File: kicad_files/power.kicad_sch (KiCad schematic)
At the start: 0 parts

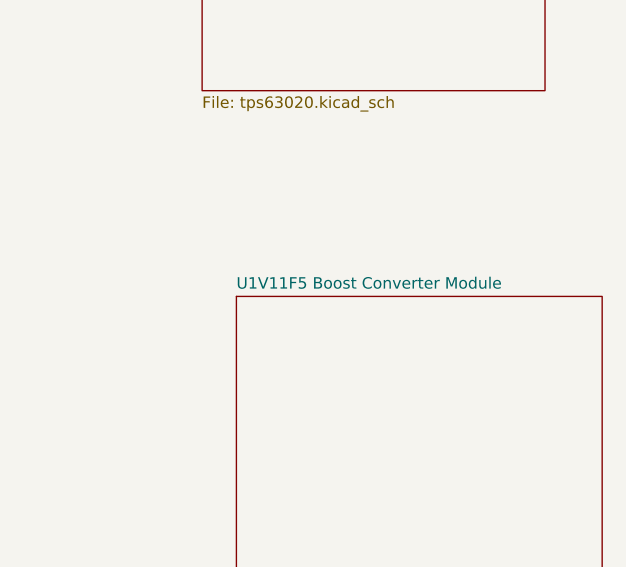
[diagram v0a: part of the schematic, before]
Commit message: Completed fuel gauge schematic based on application guidance provided in the LC709203F datasheet.
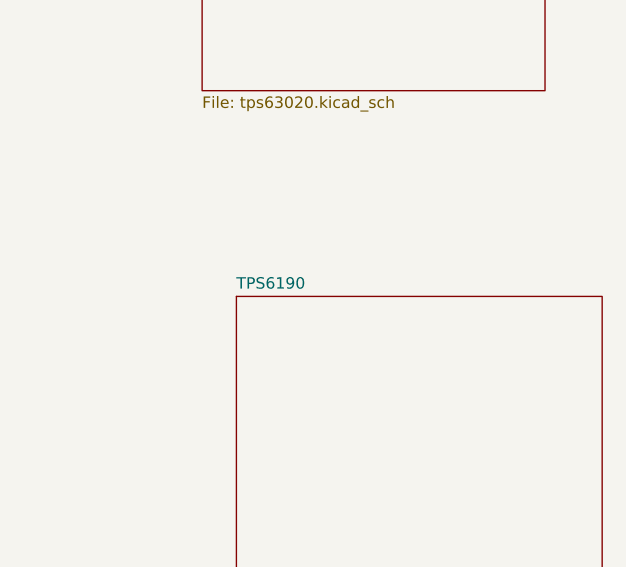
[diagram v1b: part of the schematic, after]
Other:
- sheet U1V11F5 Boost Converter Module renamed TPS6190
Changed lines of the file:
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@@
 			(color 0 0 0 0.0000)
 		)
-		(property "Sheetname" "U1V11F5 Boost Converter Module"
+		(property "Sheetname" "TPS6190"
 			(at 173.99 100.8884 0)
 			(effects

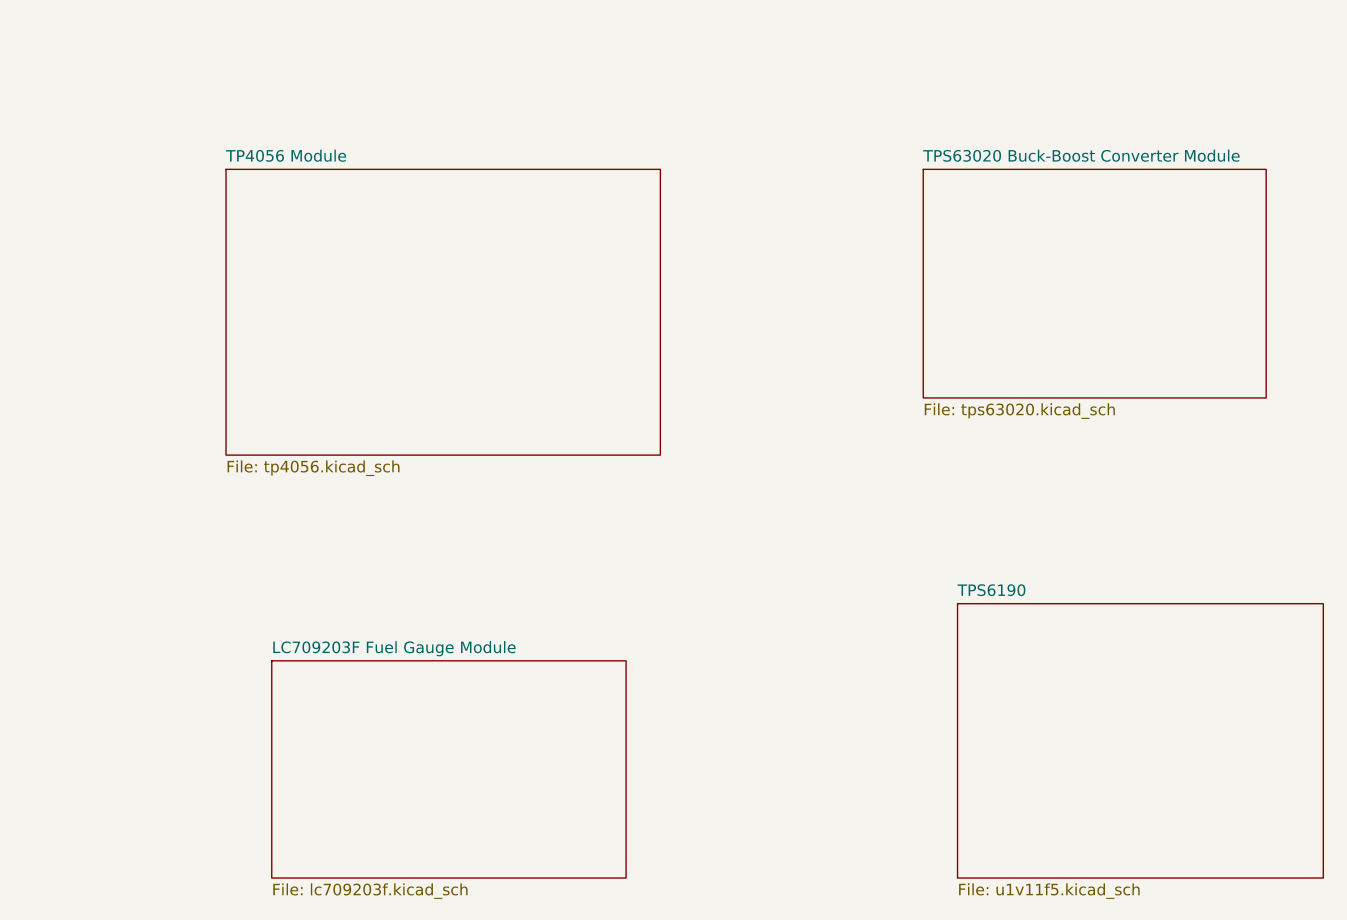
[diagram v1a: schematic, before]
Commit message: Revamped power subsystem design
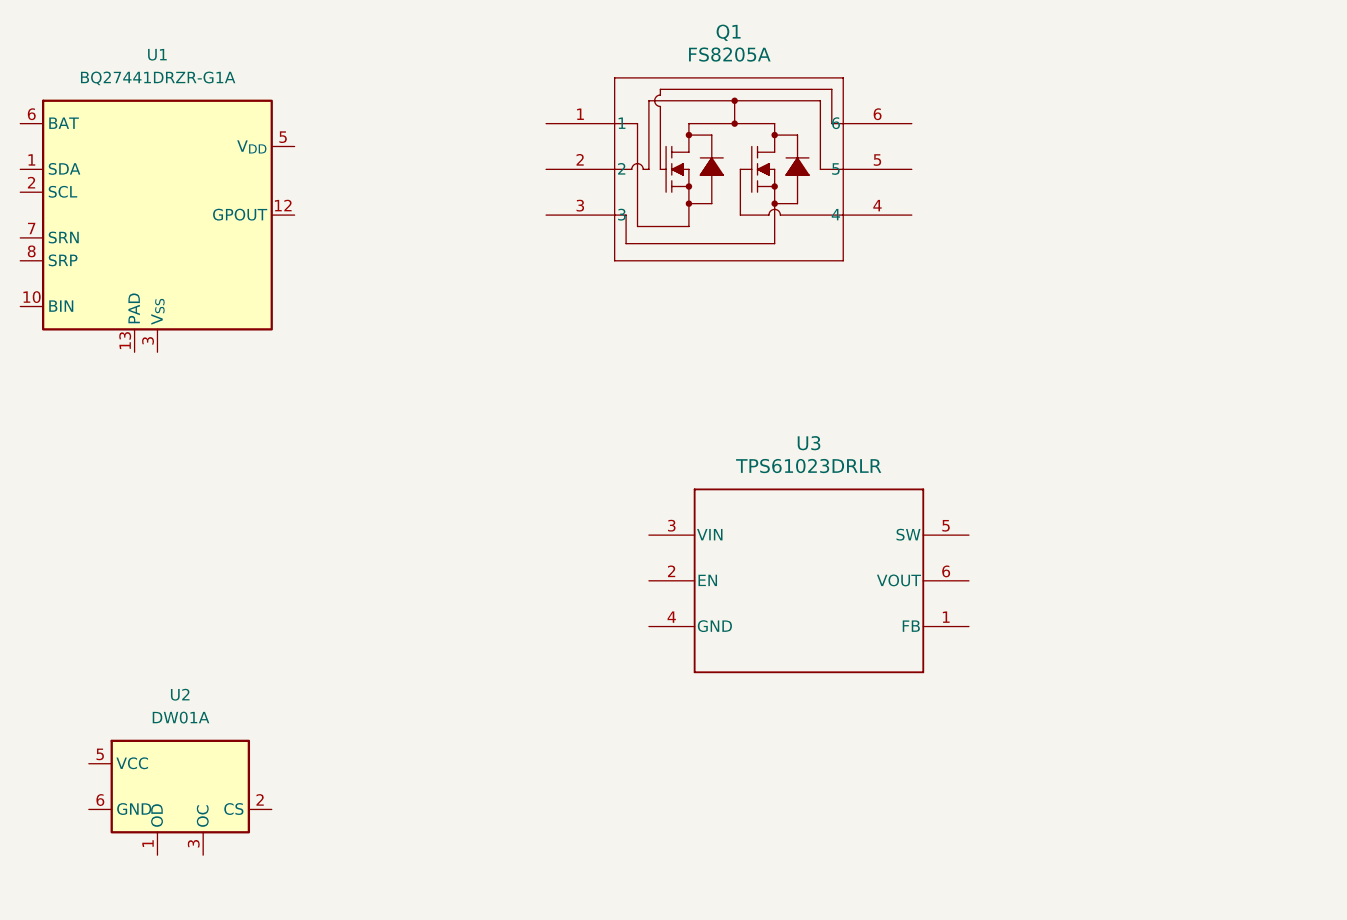
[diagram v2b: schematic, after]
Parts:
- added Q1: FS8205A, SOT-23-6L_TCP, symbol FS8205A:FS8205A
- added U1: BQ27441DRZR-G1A, Package_SON:Texas_S-PDSO-N12, symbol Battery_Management:BQ27441DRZR-G1A
- added U2: DW01A, Package_TO_SOT_SMD:SOT-23-6, symbol Battery_Management:DW01A
- added U3: TPS61023DRLR, DRL0006A, symbol TPS61023:TPS61023DRLR
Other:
- removed sheet LC709203F Fuel Gauge Module
- removed sheet TP4056 Module
- removed sheet TPS6190
- removed sheet TPS63020 Buck-Boost Converter Module

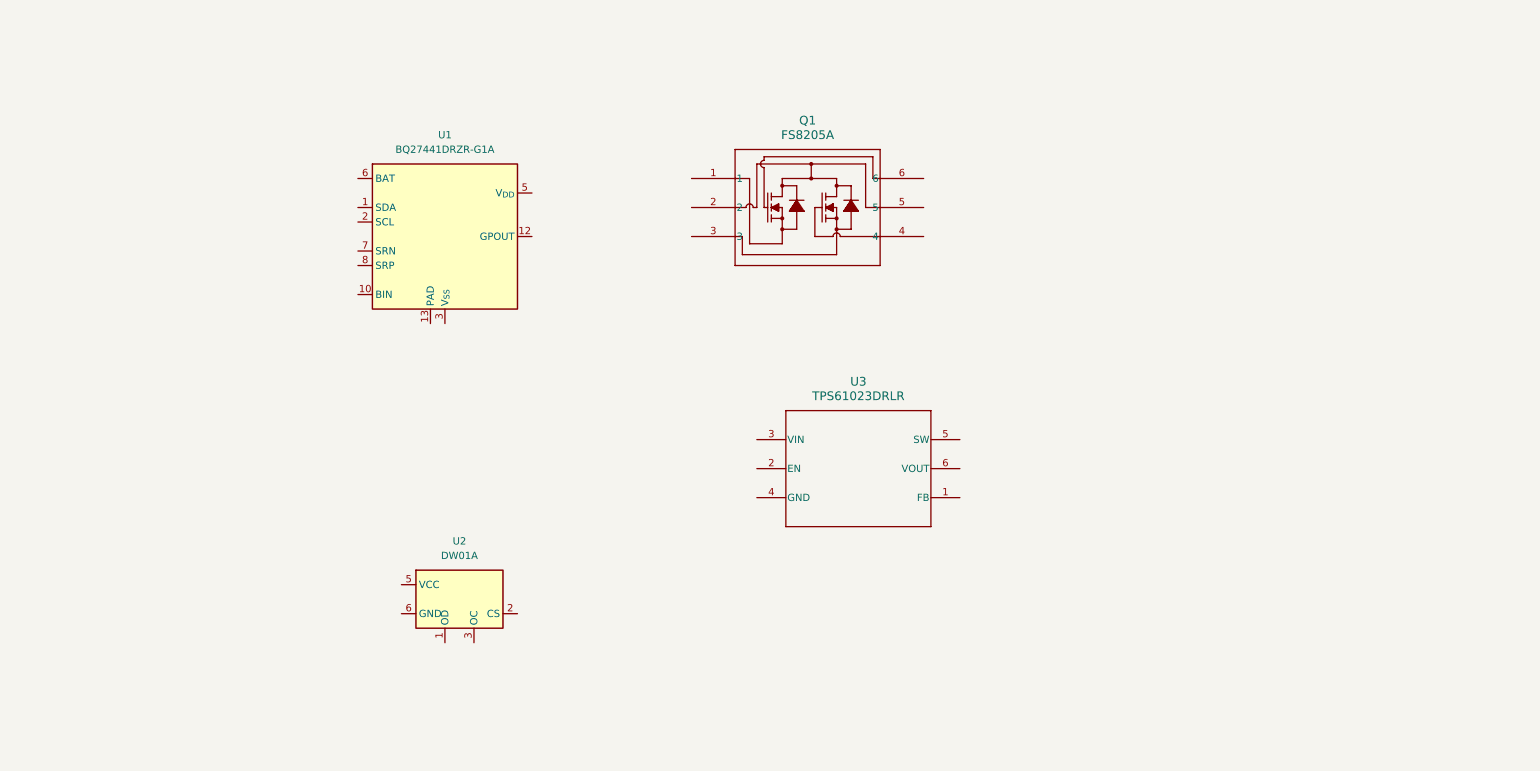
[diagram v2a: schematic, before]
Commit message: Protection portion of power subsystem
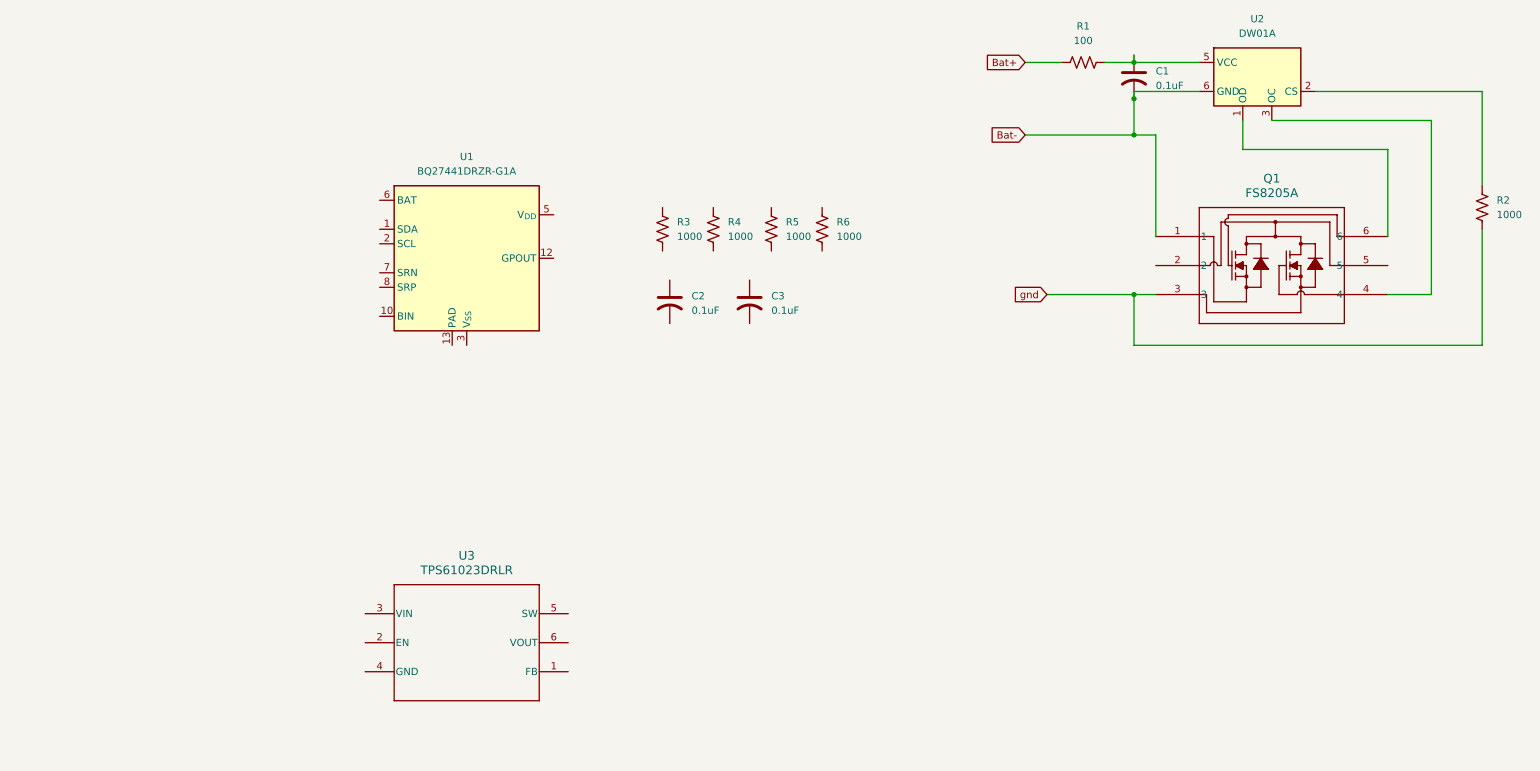
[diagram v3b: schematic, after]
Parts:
- added C1, C2, C3: 0.1uF, symbol Device:C_US
- added R1: 100, symbol Device:R_US
- added R2, R3, R4, R5, R6: 1000, symbol Device:R_US
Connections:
- net at U2.1 (OD): now also Q1.6
- net at U2.2 (CS): now also R2.1
- net at U2.3 (OC): now also Q1.4
- net at U2.5 (VCC): now also C1.1, R1.1
- net Bat-: now reaches U2.6 (GND)
- net Bat-: now also Q1.1, C1.2
- net gnd: now reaches Q1.3
- net gnd: now also R2.2
- new net Bat+: R1.2
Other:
- moved on the sheet: Q1, U1, U2, U3

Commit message: Initial power system implementation
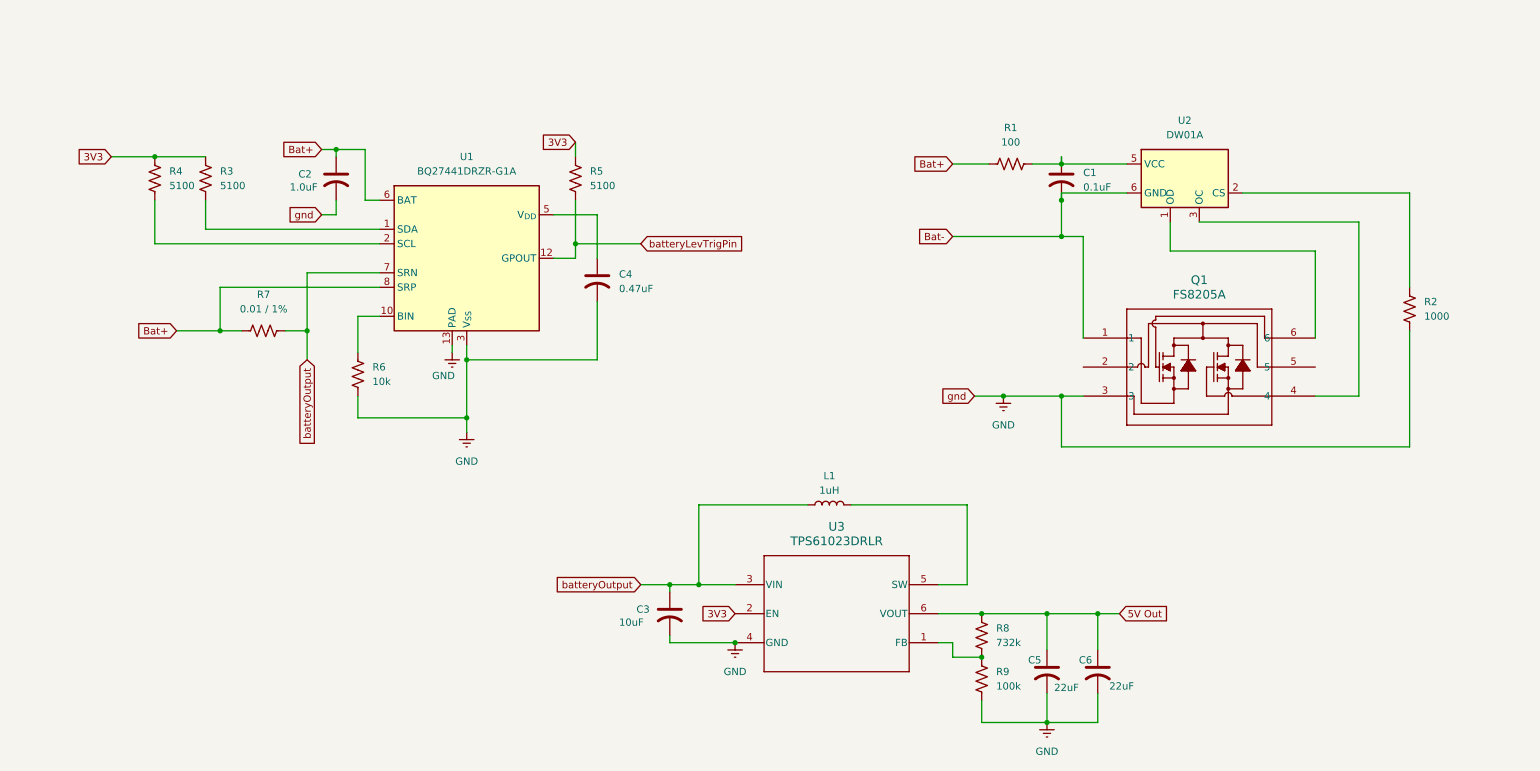
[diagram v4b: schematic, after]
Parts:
- added C4: 0.47uF, symbol Device:C_US
- added C5, C6: 22uF, symbol Device:C_US
- added L1: 1uH, symbol Device:L
- added R7: 0.01 / 1%, symbol Device:R_US
- added R8: 732k, symbol Device:R_US
- added R9: 100k, symbol Device:R_US
- C2: value 0.1uF -> 1.0uF
- C3: value 0.1uF -> 10uF
- R3, R4, R5: value 1000 -> 5100
- R6: value 1000 -> 10k
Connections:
- net gnd is gone; now on net GND: Q1.3, R2.2
- net Bat+: now also C2.1, U1.6 (BAT), U1.8 (SRP), R7.2
- net 3V3: now reaches R3.1
- net 3V3: now also R4.1, R5.1, U3.2 (EN)
- net at R3.2: now also U1.1 (SDA)
- net at U1.10 (BIN): now also R6.1
- net batteryLevTrigPin: now reaches U1.12 (GPOUT)
- net batteryLevTrigPin: now also R5.2
- net GND: now reaches U1.13 (PAD)
- net GND: now also C2.2, C3.2, R6.2, U1.3 (V_{SS}), U3.4 (GND), C4.2, C5.2, C6.2, R9.2
- net at U1.2 (SCL): now also R4.2
- net at U1.5 (V_{DD}): now also C4.1
- net batteryOutput: now reaches U1.7 (SRN)
- net batteryOutput: now also C3.1, U3.3 (VIN), L1.1, R7.1
- net at U3.1 (FB): now also R8.2, R9.1
- net at U3.5 (SW): now also L1.2
- net 5V Out: now reaches U3.6 (VOUT)
- net 5V Out: now also C5.1, C6.1, R8.1
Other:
- moved on the sheet: C1, C2, Q1, R1, R2, R3, R4, R5, R6, U2, U3

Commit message: Hierarchical labels finished. Flyback diode issue fixed. I2C pins added
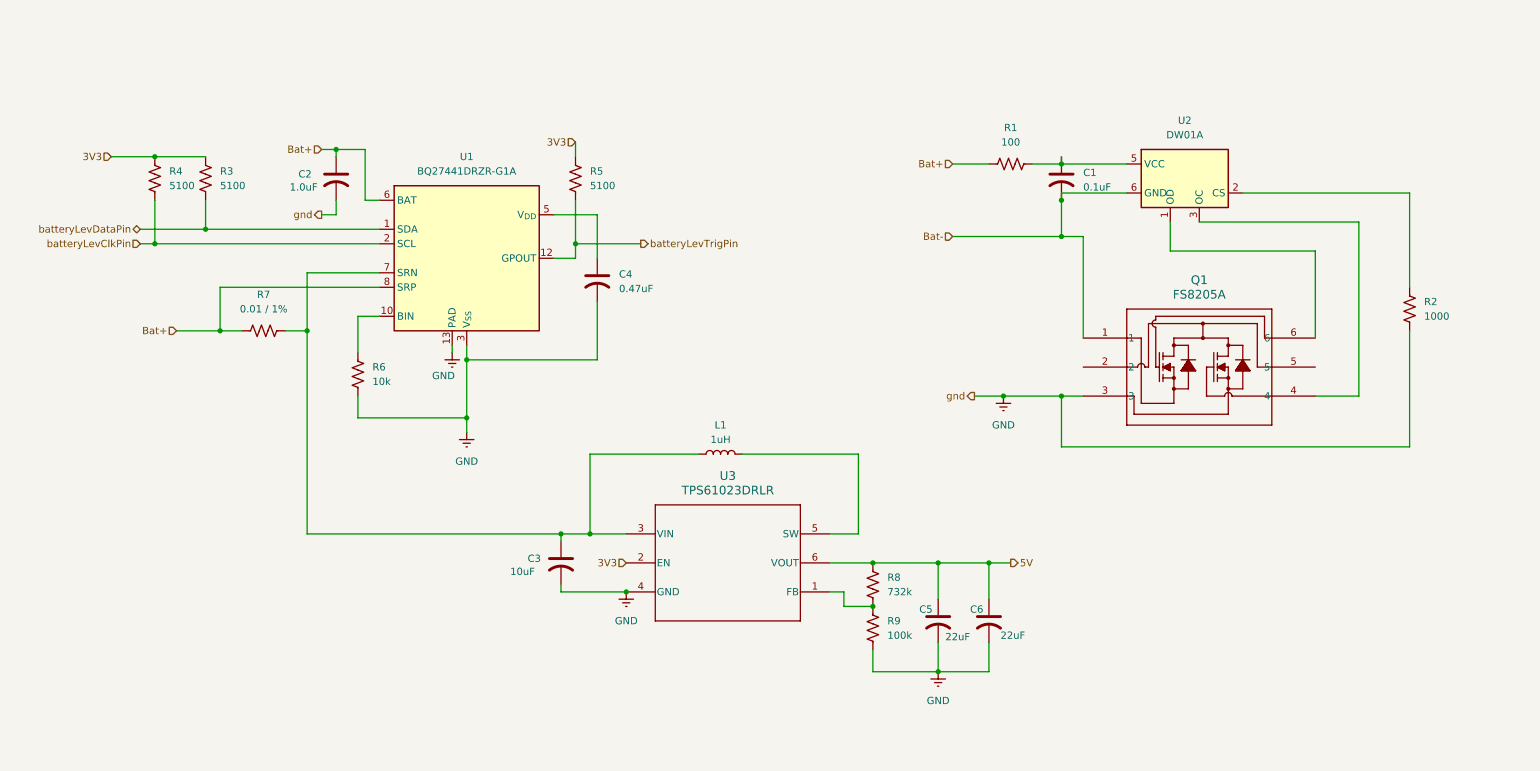
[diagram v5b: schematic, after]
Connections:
- net batteryLevDataPin: now reaches R3.2, U1.1 (SDA)
- net batteryLevClkPin: now reaches R4.2, U1.2 (SCL)
- net 5V Out renamed 5V
- net batteryOutput: no longer names the net of C3.1, L1.1, R7.1, U1.7 (SRN), U3.3 (VIN)
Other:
- moved on the sheet: C3, C5, C6, L1, R8, R9, U3

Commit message: Partial footprint assignment
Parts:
- Q1: footprint SOT-23-6L_TCP -> Fs8205a:SOT-23-6L_TCP
- U3: footprint DRL0006A -> TPS61023:DRL0006A
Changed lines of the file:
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@@
 			)
 		)
-		(property "Footprint" "SOT-23-6L_TCP"
+		(property "Footprint" "Fs8205a:SOT-23-6L_TCP"
 			(at 196.85 76.2 0)
 			(effects
@@
 			)
 		)
-		(property "Footprint" "DRL0006A"
+		(property "Footprint" "TPS61023:DRL0006A"
 			(at 134.62 115.57 0)
 			(effects
